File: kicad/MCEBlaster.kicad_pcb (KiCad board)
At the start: 2 copper layers, 30 x 67.7 mm, 16 parts, among them J1 DB9_Male_MountingHoles, J2 Conn_01x02_Male, J3 DB15_Male_HighDensity_Mountin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, J6 Conn_01x06_Male, SW1 AUTO_ADJUST, SW2 PX_CLK_BTN, U1 74LS245, U2 RaspberryPi_Pico

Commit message: PCB rev0.2
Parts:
- removed SW1: AUTO_ADJUST, Button_Switch_THT:SW_PUSH_6mm
- removed SW2: PX_CLK_BTN, Button_Switch_THT:SW_PUSH_6mm
- added AUTO_ADJUST: AUTO_ADJUST, Button_Switch_THT:SW_PUSH_6mm, B.Cu at (123.7, 40.9)
- added BLU: 1K, Potentiometer_THT:Potentiometer_Runtron_RM-065_Vertical, B.Cu at (123.4, 23.9)
- added GRN: 1K, Potentiometer_THT:Potentiometer_Runtron_RM-065_Vertical, B.Cu at (128.5, 31.2)
- added PXL_CLK: PXL_CLK, Button_Switch_THT:SW_PUSH_6mm, B.Cu at (131.8, 40.9)
- added RED: 1K, Potentiometer_THT:Potentiometer_Runtron_RM-065_Vertical, B.Cu at (131.6, 23.9)
- C1: footprint Capacitor_SMD:C_1206_3216Metric_Pad1.33x1.80mm_HandSolder -> Capacitor_THT:C_Disc_D4.3mm_W1.9mm_P5.00mm; moved to B.Cu
- J6: moved to F.Cu
- R2, R5, R7: value 845 -> 780; footprint Resistor_SMD:R_1206_3216Metric_Pad1.30x1.75mm_HandSolder -> Resistor_THT:R_Axial_DIN0207_L6.3mm_D2.5mm_P10.16mm_Horizontal; moved to B.Cu
- R3, R4, R6: value 422 -> 390; footprint Resistor_SMD:R_1206_3216Metric_Pad1.30x1.75mm_HandSolder -> Resistor_THT:R_Axial_DIN0207_L6.3mm_D2.5mm_P10.16mm_Horizontal; moved to B.Cu
- U1: value 74LS245 -> 74FCT245; footprint Package_SO:SO-20_12.8x7.5mm_P1.27mm -> Package_DIP:DIP-20_W7.62mm_Socket; moved to F.Cu
- moved J6 18.8 mm to (112.8, 19.8), turned to 0 degrees
- moved C1 11.8 mm to (118.4, 67.3), turned to 90 degrees
- moved R4 10.4 mm to (136.8, 44.5), turned to -90 degrees
- moved R5 10.1 mm to (131.7, 44.3), turned to -90 degrees
- moved R3 8.90 mm to (113.0, 57.1)
- moved R7 8.82 mm to (136.8, 57.2)
- moved R6 6.93 mm to (131.7, 57.0), turned to -90 degrees
- moved R2 6.37 mm to (113.0, 54.6)
- moved U1 5.21 mm to (128.8, 66.8), turned to 180 degrees
- moved J2 3.02 mm to (137.4, 34.3)
- moved D1 2.92 mm to (137.4, 23.5)
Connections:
- J3 pad 11: (no net) -> unconnected-(J3-Pad11)
- J3 pad 12: (no net) -> unconnected-(J3-Pad12)
- J3 pad 15: (no net) -> unconnected-(J3-Pad15)
- J3 pad 4: (no net) -> unconnected-(J3-Pad4)
- J3 pad 9: (no net) -> unconnected-(J3-Pad9)
- R2 pad 1: VGA_B -> BOUT
- R3 pad 1: VGA_B -> BOUT
- R4 pad 1: VGA_R -> ROUT
- R5 pad 1: VGA_R -> ROUT
- R6 pad 1: VGA_G -> GOUT
- R7 pad 1: VGA_G -> GOUT
- U2 pad 30: (no net) -> unconnected-(U2-RUN-Pad30)
- U2 pad 35: (no net) -> unconnected-(U2-ADC_VREF-Pad35)
- U2 pad 37: (no net) -> unconnected-(U2-3V3_EN-Pad37)
- U2 pad 40: (no net) -> unconnected-(U2-VBUS-Pad40)
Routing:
- net BOUT: track 0.00 -> 49.7 mm, vias 0 -> 1
- net VGA_B: track 62.0 -> 20.5 mm, vias 0 -> 1
- net GND: track 205.6 -> 244.8 mm, vias 9 -> 12
- net GOUT: track 0.00 -> 38.0 mm
- net ROUT: track 0.00 -> 28.2 mm
- net SB: track 78.5 -> 53.5 mm, vias 1 -> 0
- net TTL_SG: track 7.51 -> 31.5 mm
- net VGA_V: track 58.0 -> 81.4 mm, vias 1 -> 0
- net TTL_SR: track 4.71 -> 25.7 mm
- net VGA_R: track 41.9 -> 22.7 mm, vias 1 -> 0
- net VGA_G: track 56.0 -> 36.8 mm
- net TTL_SB: track 8.25 -> 27.0 mm
- net TTL_PR: track 4.81 -> 22.6 mm
- net Net-(U2-GP14): track 6.56 -> 21.7 mm
- net SG_INT: track 70.1 -> 55.0 mm
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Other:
- net class Default removed
- board text added: "+"
- board text added: "390"
- board text added: "74FCT245"
- board text added: "780"
- board text added: "MCEBlaster rev0.2"
- board text added: "VGA Connector Bottom"
- board text added: "VGA Connector Top"
- board text removed: "422"
- board text removed: "74LVC245"
- board text removed: "AUTO ADJUST"
- board text removed: "MCEBlaster rev0.1"
- board text removed: "PIXEL CLOCK"

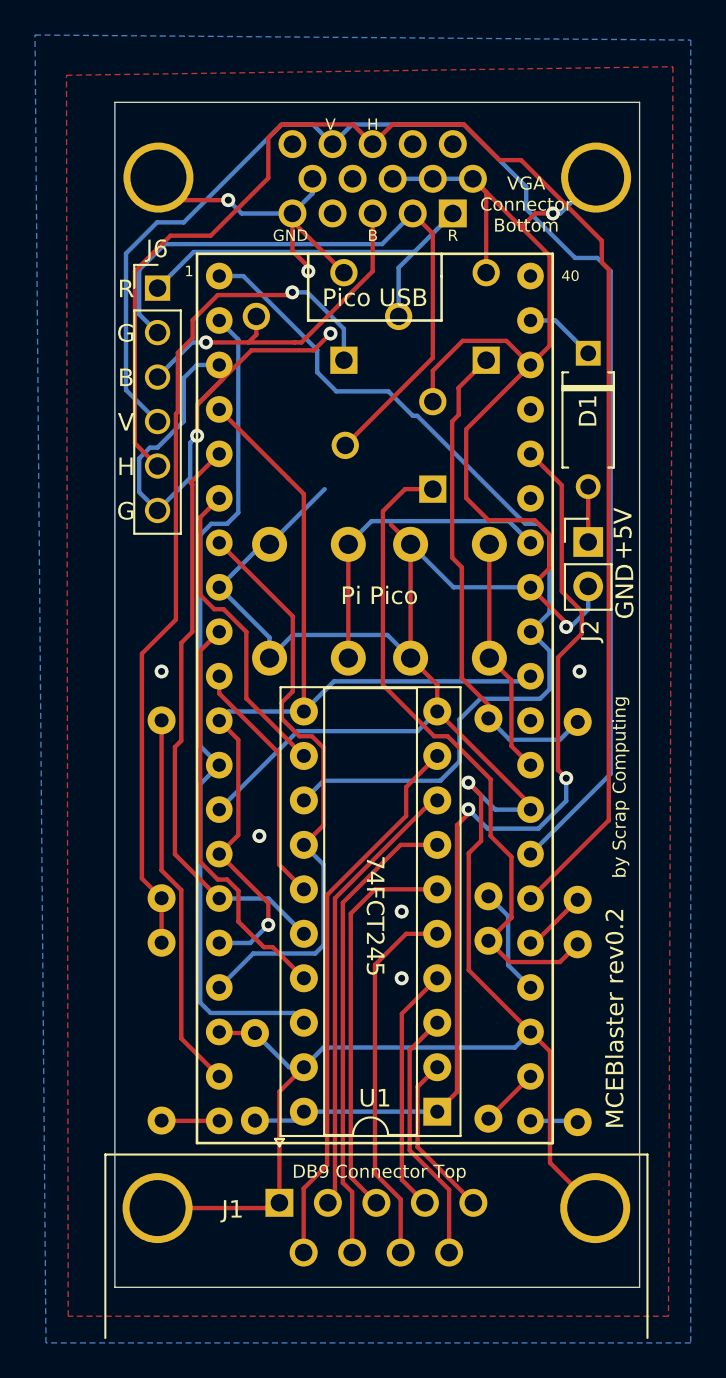
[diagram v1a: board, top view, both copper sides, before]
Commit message: PCB Rev 0.3
Updates the VGA connector footprint. Should accept both "short" and "long" connectors.
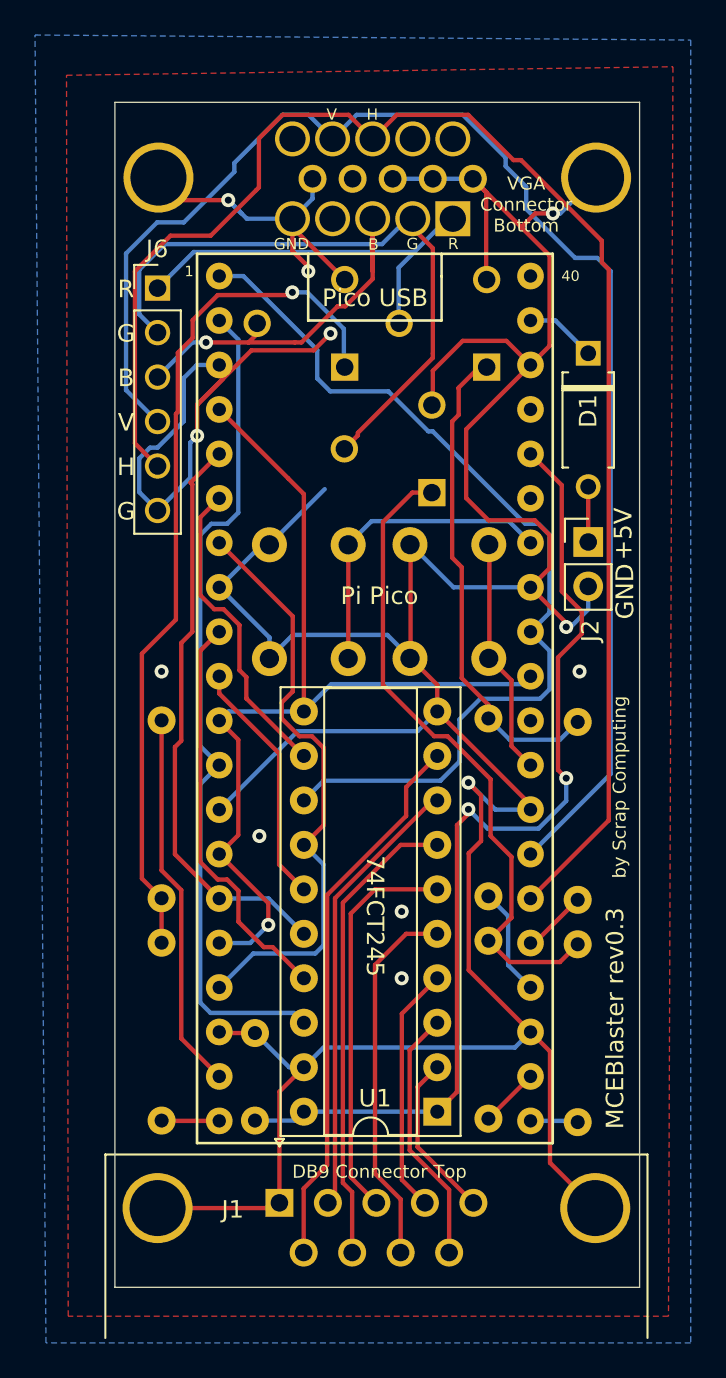
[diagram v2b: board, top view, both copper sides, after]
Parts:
- removed AUTO_ADJUST: AUTO_ADJUST, Button_Switch_THT:SW_PUSH_6mm
- removed BLU, GRN, RED: 1K, Potentiometer_THT:Potentiometer_Runtron_RM-065_Vertical
- removed PXL_CLK: PXL_CLK, Button_Switch_THT:SW_PUSH_6mm
- added AUTO_ADJUST1: AUTO_ADJUST, Button_Switch_THT:SW_PUSH_6mm, B.Cu at (123.7, 40.9)
- added BLU1: 1K, Potentiometer_THT:Potentiometer_Runtron_RM-065_Vertical, B.Cu at (123.5, 24.3)
- added GRN1: 1K, Potentiometer_THT:Potentiometer_Runtron_RM-065_Vertical, B.Cu at (128.5, 31.4)
- added PXL_CLK1: PXL_CLK, Button_Switch_THT:SW_PUSH_6mm, B.Cu at (131.7, 40.9)
- added RED1: 1K, Potentiometer_THT:Potentiometer_Runtron_RM-065_Vertical, B.Cu at (131.6, 24.3)
- J3: footprint Connector_Dsub:DSUB-15-HD_Female_Horizontal_P2.29x1.98mm_EdgePinOffset3.03mm_Housed_MountingHolesOffset4.94mm -> MCEBlaster:VGA_connector_both_short_and_long
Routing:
- net VGA_B: track 20.5 -> 23.8 mm
- net VGA_V: track 81.4 -> 82.7 mm
- net VGA_H: track 86.4 -> 87.4 mm
- net GND: track 244.8 -> 245.6 mm
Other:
- board text added: "1K"
- board text added: "AUTO_ADJUST"
- board text added: "BLUE"
- board text added: "GRN"
- board text added: "MCEBlaster rev0.3"
- board text added: "PX_CLK"
- board text added: "RED"
- board text removed: "MCEBlaster rev0.2"
